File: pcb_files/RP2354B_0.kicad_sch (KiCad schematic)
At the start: 31 parts

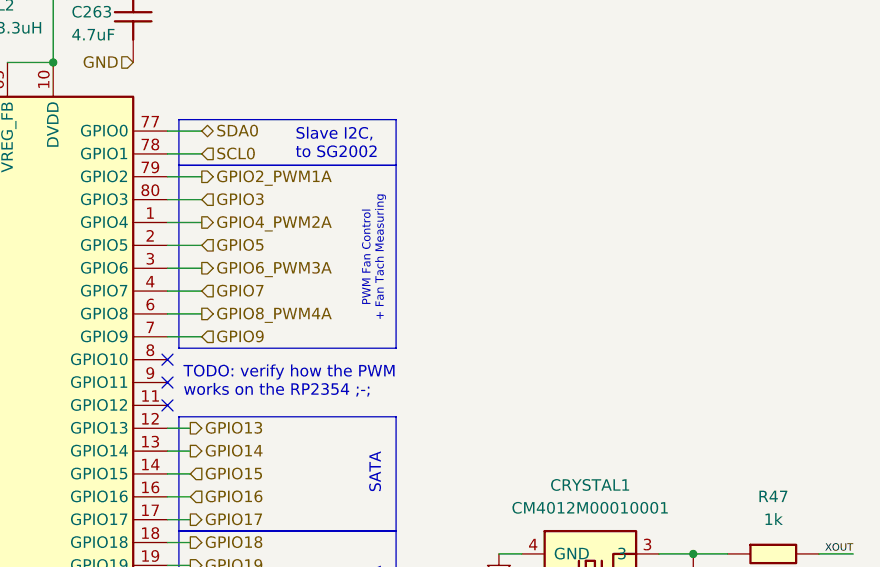
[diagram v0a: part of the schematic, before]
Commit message: Added FAN4 and updated RP2354/PAC1954 to match
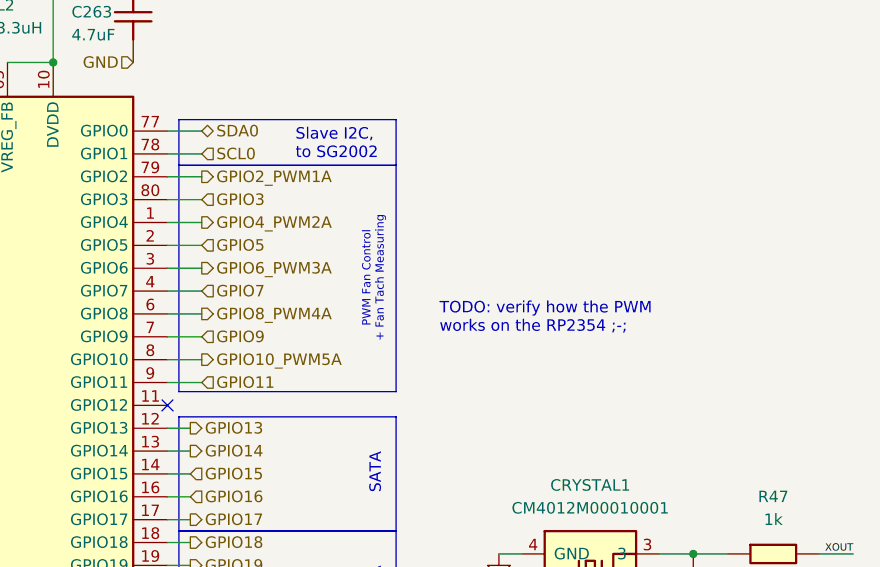
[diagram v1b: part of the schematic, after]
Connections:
- net GPIO10_PWM5A: now reaches PI1.8 (GPIO10)
- net GPIO11: now reaches PI1.9 (GPIO11)
- no-connect marks 14 -> 12
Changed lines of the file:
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@@
 	(rectangle
 		(start 129.54 40.64)
-		(end 153.67 60.96)
+		(end 153.67 65.786)
 		(stroke
 			(width 0)
@@
 	(text "TODO: verify how the PWM\nworks on the RP2354 ;-;"
 		(exclude_from_sim no)
-		(at 130.048 64.77 0)
+		(at 158.496 57.658 0)
 		(effects
 			(font
@@
 	(text "PWM Fan Control\n+ Fan Tach Measuring"
 		(exclude_from_sim no)
-		(at 151.13 51.054 90)
+		(at 151.13 53.34 90)
 		(effects
 			(font
@@
 	)
 	(no_connect
-		(at 128.27 64.77)
-	)
-	(no_connect
 		(at 128.27 113.03)
 	)
@@
 	)
 	(no_connect
-		(at 128.27 62.23)
-	)
-	(no_connect
 		(at 77.47 59.69)
 	)
@@
 	(wire
 		(pts
+			(xy 128.27 62.23) (xy 132.08 62.23)
+		)
+		(stroke
+			(width 0)
+			(type default)
+		)
+	)
+	(wire
+		(pts
 			(xy 102.87 161.29) (xy 109.22 161.29)
 		)
@@
 		(pts
 			(xy 160.02 151.13) (xy 170.18 151.13)
+		)
+		(stroke
+			(width 0)
+			(type default)
+		)
+	)
+	(wire
+		(pts
+			(xy 128.27 64.77) (xy 132.08 64.77)
 		)
 		(stroke
@@
 		)
 	)
+	(hierarchical_label "GPIO10_PWM5A"
+		(shape output)
+		(at 132.08 62.23 0)
+		(effects
+			(font
+				(size 1.27 1.27)
+			)
+			(justify left)
+		)
+	)
 	(hierarchical_label "GPIO9"
 		(shape input)
@@
 		(effects
 			(font
+				(size 1.27 1.27)
+			)
+			(justify left)
+		)
+	)
+	(hierarchical_label "GPIO11"
+		(shape input)
+		(at 132.08 64.77 0)
+		(effects
+			(font
